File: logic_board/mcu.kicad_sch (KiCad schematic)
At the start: 24 parts, among them J2 SOICBite, SW1 SW_Push, SW2 SW_Push, SW3 SW_Push, SW4 SW_Push, U1 STM32H7B0RBTx, Y1 Crystal_GND24

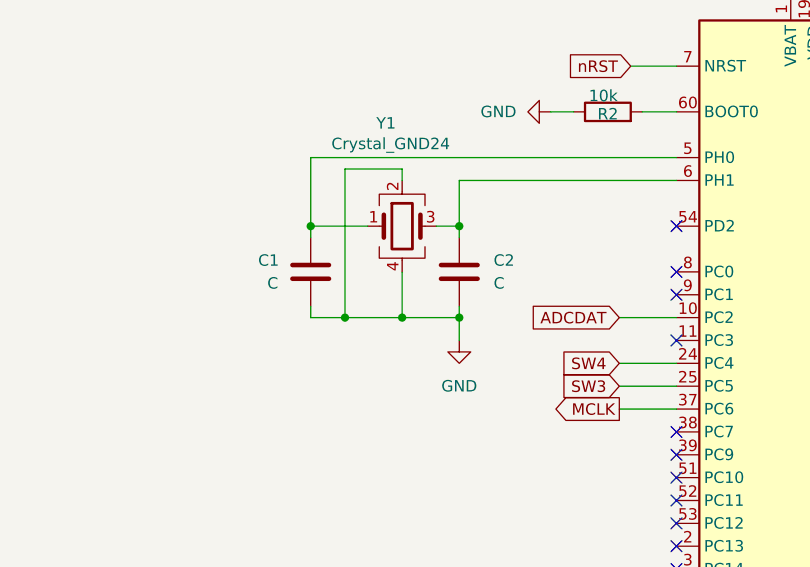
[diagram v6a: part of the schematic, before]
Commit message: Fix some incorrect footprints/symbols
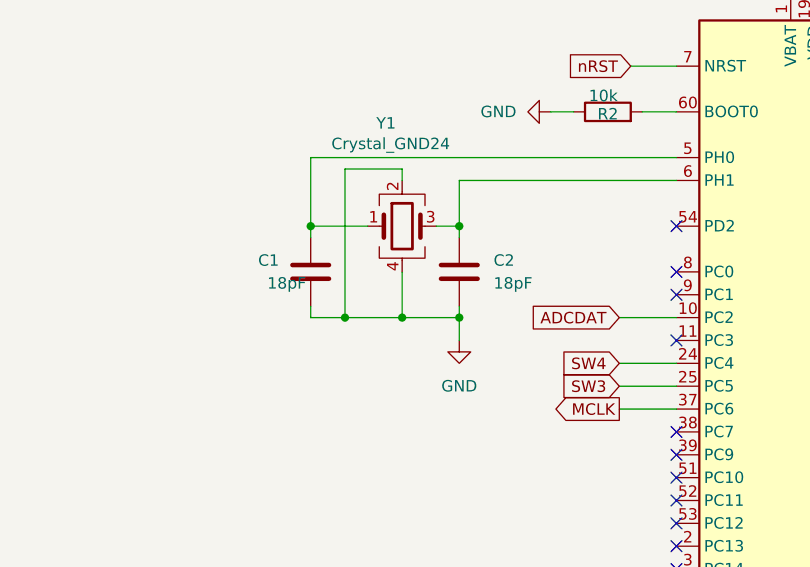
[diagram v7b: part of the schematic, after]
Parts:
- C1, C2: value C -> 18pF
- RN2, RN3: footprint Resistor_SMD:R_Array_Concave_4x0402 -> Resistor_SMD:R_Array_Concave_4x0603
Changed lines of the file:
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@@
 			)
 		)
-		(property "Footprint" "Resistor_SMD:R_Array_Concave_4x0402"
+		(property "Footprint" "Resistor_SMD:R_Array_Concave_4x0603"
 			(at 218.44 23.495 90)
 			(effects
@@
 			)
 		)
-		(property "Value" "C"
+		(property "Value" "18pF"
 			(at 90.17 60.9599 0)
 			(effects
@@
 			)
 		)
-		(property "Footprint" "Resistor_SMD:R_Array_Concave_4x0402"
+		(property "Footprint" "Resistor_SMD:R_Array_Concave_4x0603"
 			(at 218.44 51.435 90)
 			(effects
@@
 			)
 		)
-		(property "Value" "C"
+		(property "Value" "18pF"
 			(at 65.024 60.96 0)
 			(effects

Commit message: Replace WM8904 codec with ES8388
The latter is simpler. Specifically, it doesn't require a 1.8v supply (which I had neglected to hook up). It also doesn't require a ground feedback line from the headphone outputs. It also has a beefier output stage (40mW headphone output vs. 28 @ 30 ohms for the old one)
Also changed the interface from I2S to SPI, avoiding the need for pullup resistors (also missing from previous iteration).
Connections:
- net SPI_CE: now reaches U1.20 (PA4)
- net SPI_CLK: now reaches U1.21 (PA5)
- net SPI_MOSI: now reaches U1.23 (PA7)
- net SCK: no longer names the net of U1.58 (PB6)
- net SDA: no longer names the net of U1.59 (PB7)
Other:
- moved on the sheet: C17, C18, C19, C20, C21, C22, C29
